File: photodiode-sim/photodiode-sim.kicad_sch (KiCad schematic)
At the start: 8 parts, among them Q1 2N3904

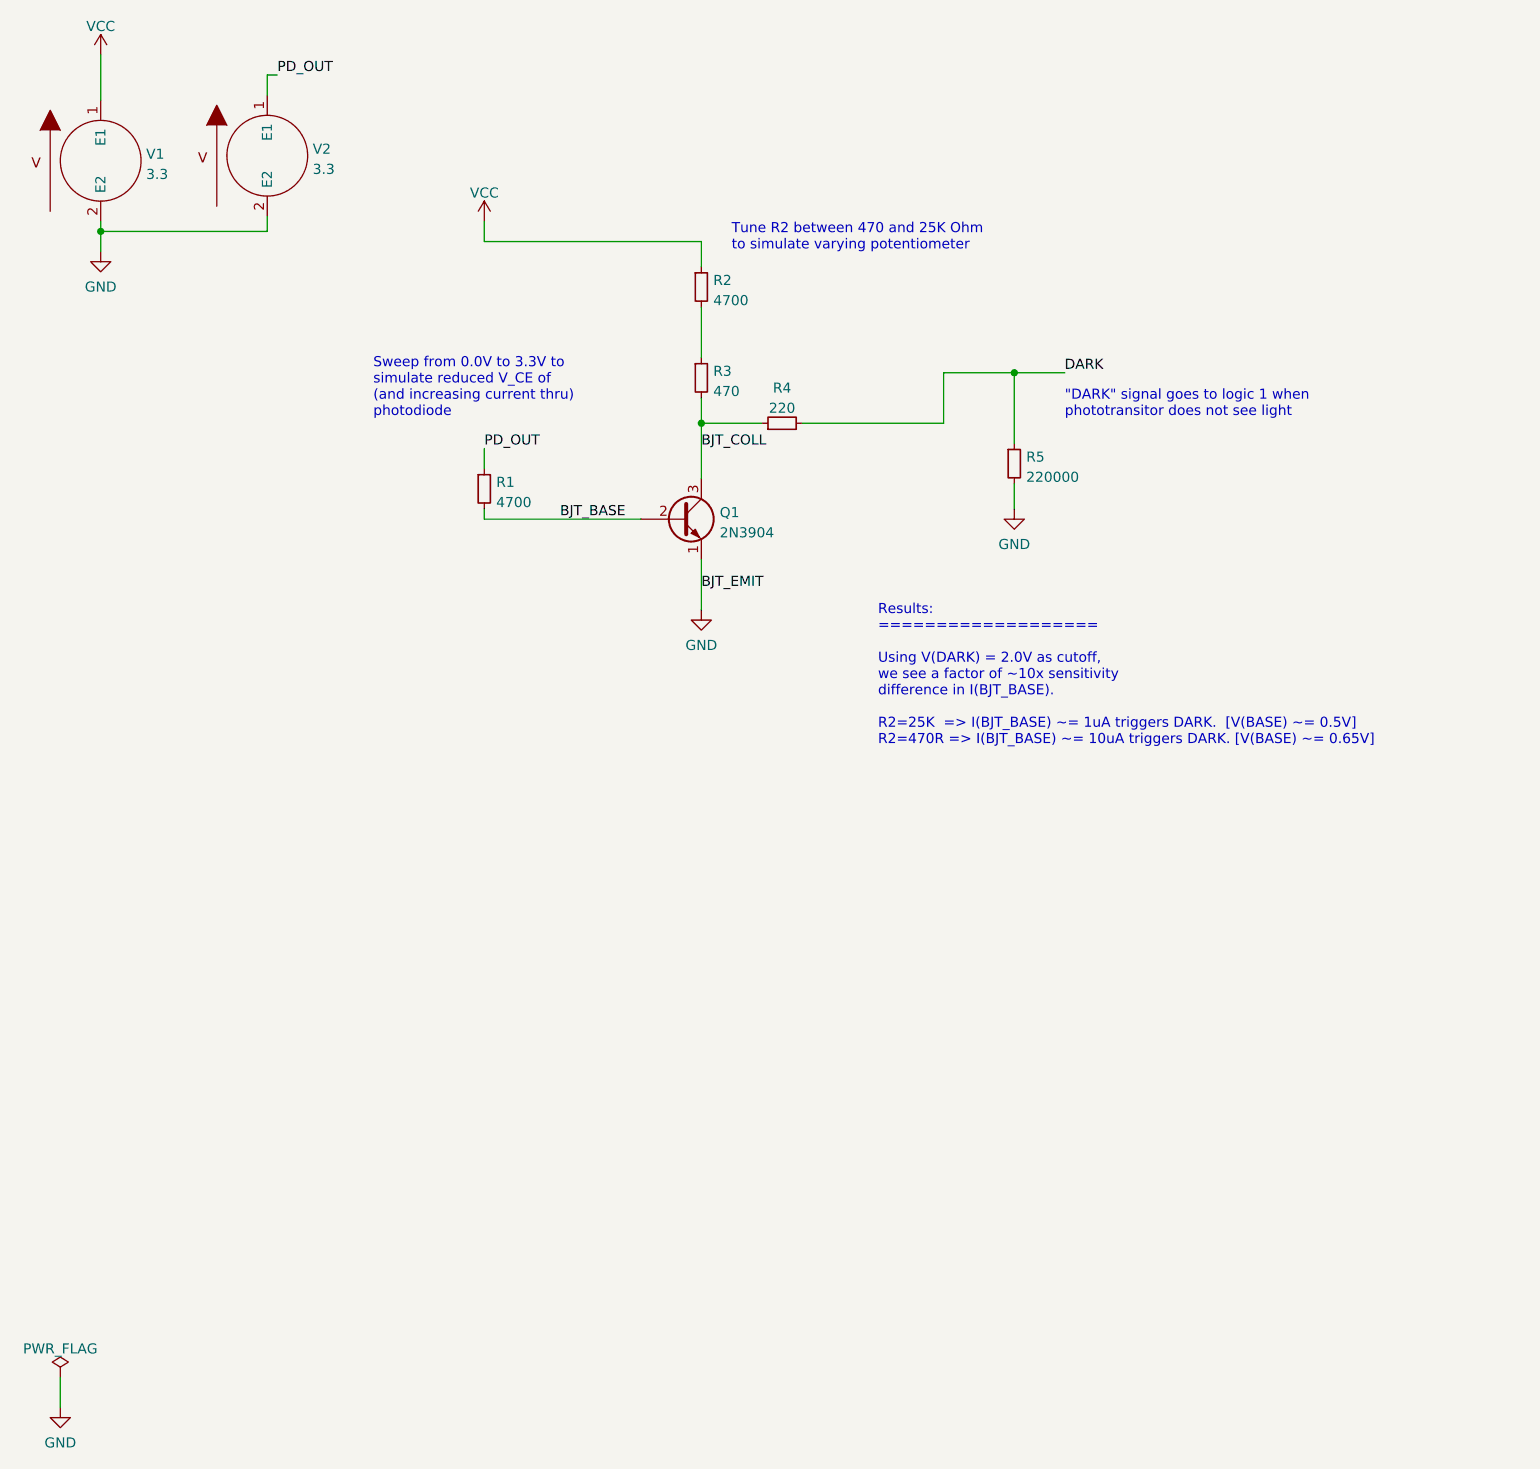
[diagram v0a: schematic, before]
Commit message: Further refinement of potentiometer model.
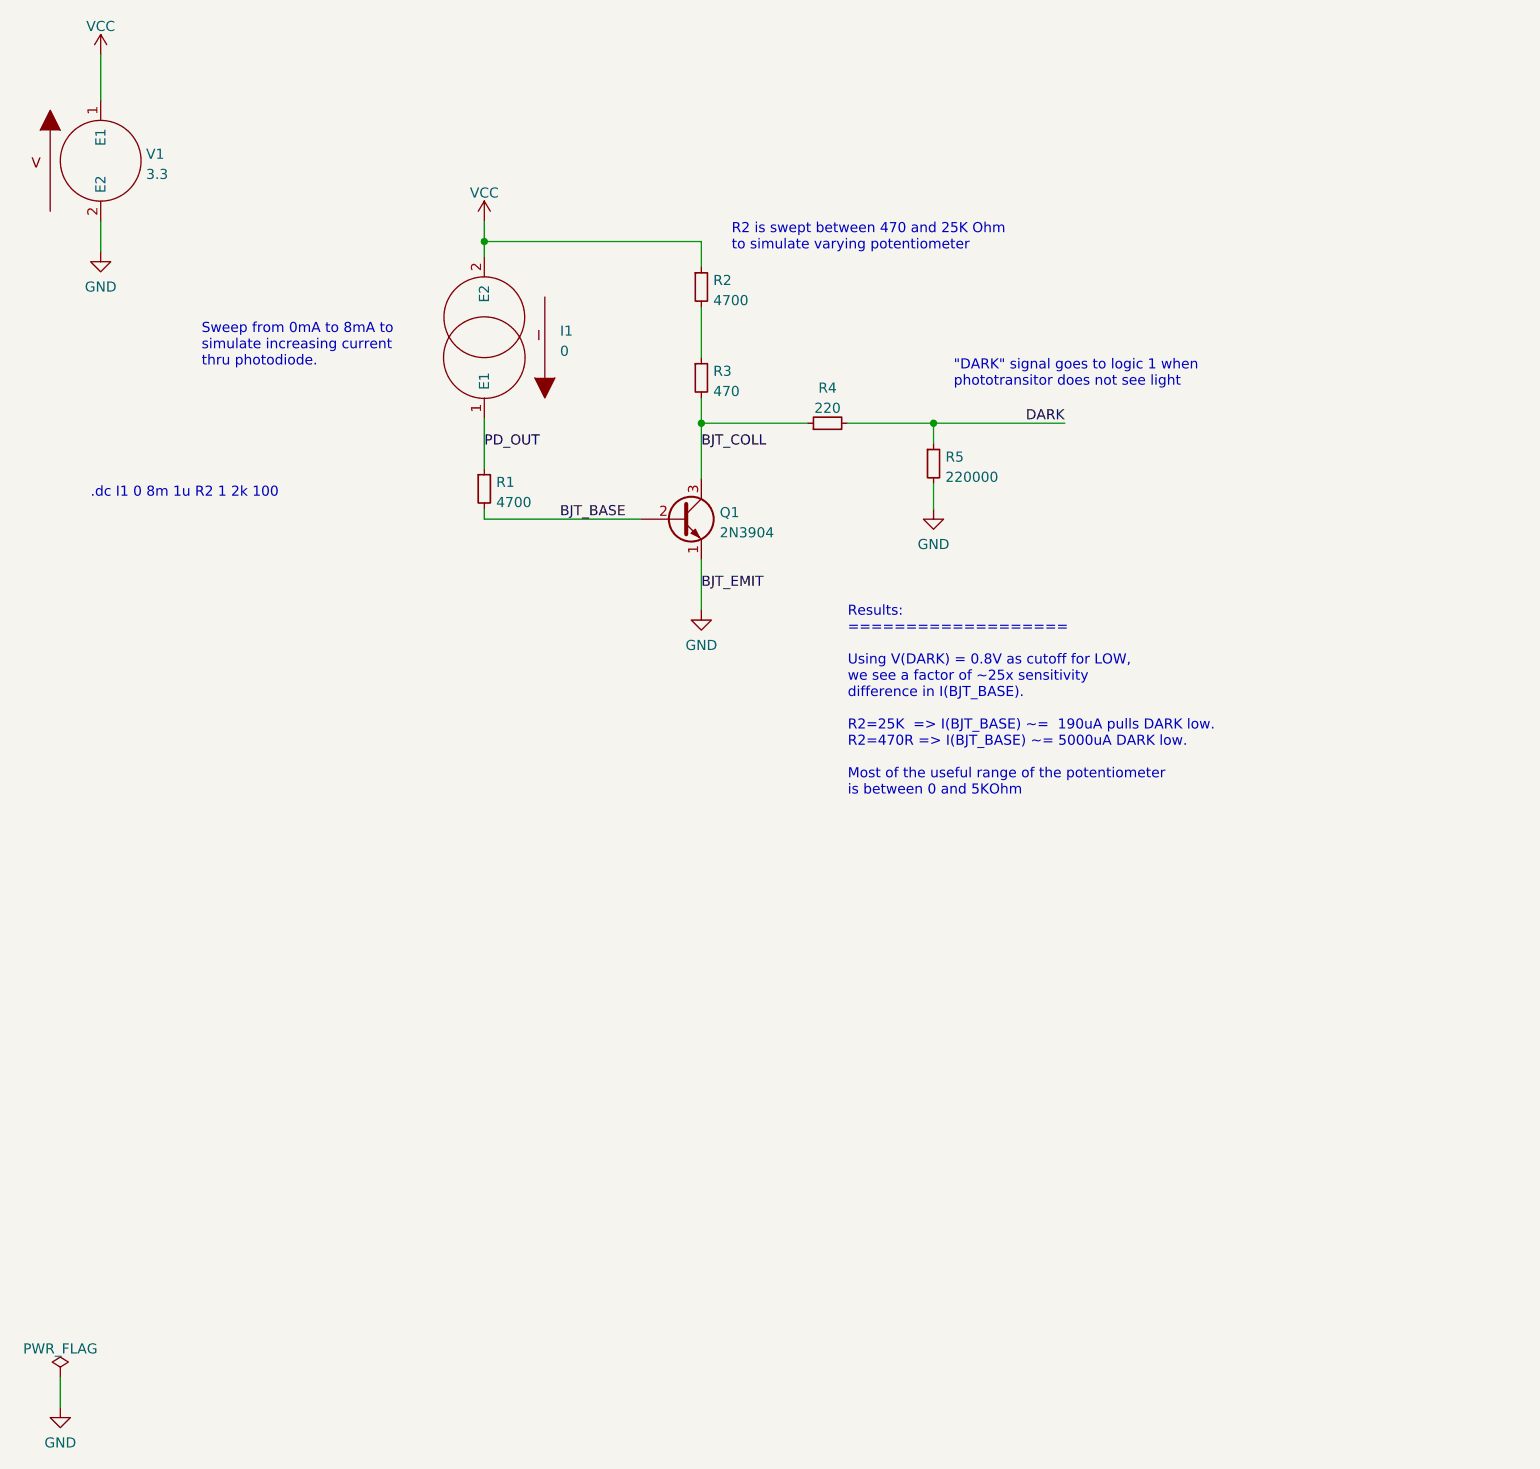
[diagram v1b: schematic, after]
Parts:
- removed V2: 3.3, symbol pspice:VSOURCE
- added I1: 0, symbol pspice:ISOURCE
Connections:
- net PD_OUT: now also I1.1 (E1)
- net VCC: now also I1.2 (E2)
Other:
- note added: ".dc I1 0 8m 1u R2 1 2k 100"
- note added: "R2 is swept between 470 and 25K Ohm to simulate varying potentiometer"
- note added: "Results: =================== Using V(DARK) = 0.8V as cutoff for LOW, we see a factor of ~25x sensitivity difference in I(BJT_BASE). R2=25K => I(BJT_BASE) ~= 190uA pulls DARK low. R2=470R => I(BJT_BASE) ~= 5000uA DARK low. Most of the useful range of the potentiometer is between 0 and 5KOhm"
- note added: "Sweep from 0mA to 8mA to simulate increasing current thru photodiode."
- note removed: "Results: =================== Using V(DARK) = 2.0V as cutoff, we see a factor of ~10x sensitivity difference in I(BJT_BASE). R2=25K => I(BJT_BASE) ~= 1uA triggers DARK. [V(BASE) ~= 0.5V] R2=470R => I(BJT_BASE) ~= 10uA triggers DARK. [V(BASE) ~= 0.65V]"
- note removed: "Sweep from 0.0V to 3.3V to simulate reduced V_CE of (and increasing current thru) photodiode"
- note removed: "Tune R2 between 470 and 25K Ohm to simulate varying potentiometer"
- moved on the sheet: R4, R5
